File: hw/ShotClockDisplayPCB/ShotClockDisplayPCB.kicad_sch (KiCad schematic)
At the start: 0 parts

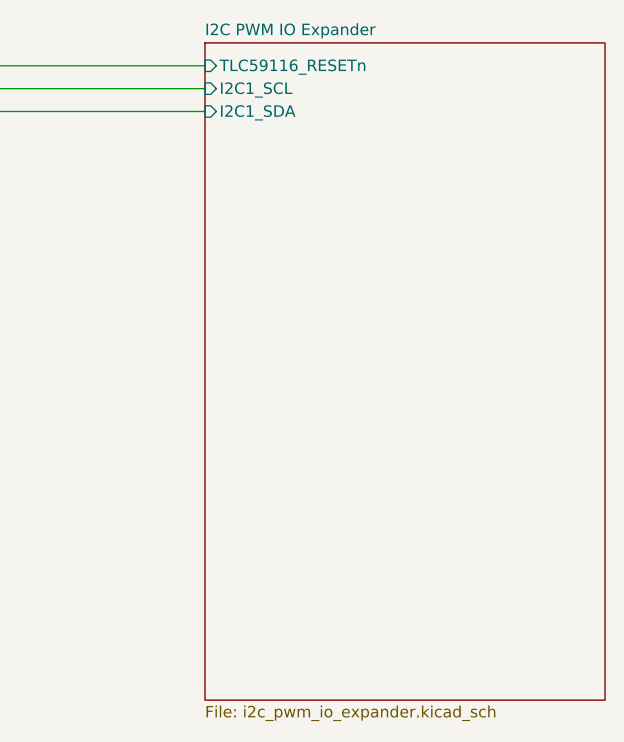
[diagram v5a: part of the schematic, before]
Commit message: Redid routing on disp PCB
Added TLC chip
Routed everything
Used way more filled areas
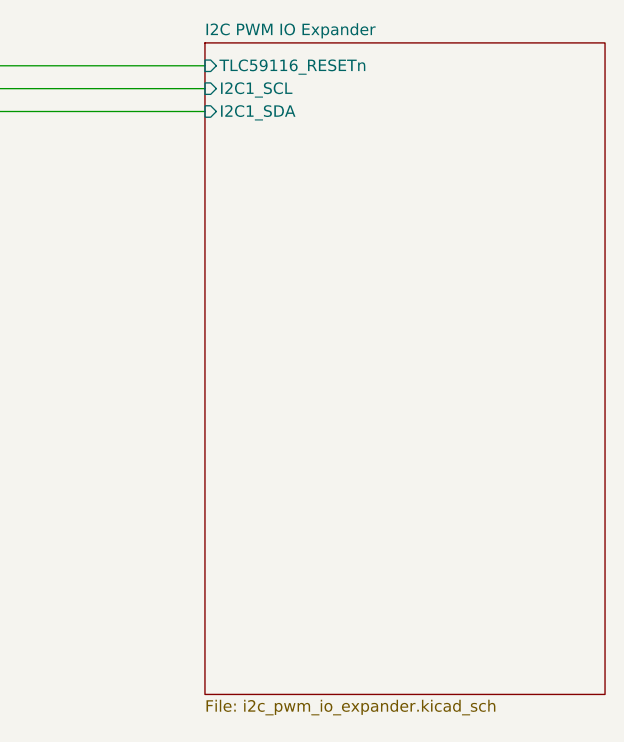
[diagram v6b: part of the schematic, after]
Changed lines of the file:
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@@
     )
   )
-  (sheet (at 140.335 54.61) (size 44.45 73.025) (fields_autoplaced)
+  (sheet (at 140.335 54.61) (size 44.45 72.39) (fields_autoplaced)
     (stroke (width 0.1524) (type solid))
     (fill (color 0 0 0 0.0000))
@@
       (effects (font (size 1.27 1.27)) (justify left bottom))
     )
-    (property "Sheetfile" "i2c_pwm_io_expander.kicad_sch" (at 140.335 128.2196 0)
+    (property "Sheetfile" "i2c_pwm_io_expander.kicad_sch" (at 140.335 127.5846 0)
       (effects (font (size 1.27 1.27)) (justify left top))
     )

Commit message: Fixed mainboard with feedback from Luc
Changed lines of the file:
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@@
     )
   )
-  (sheet (at 140.335 54.61) (size 44.45 72.39) (fields_autoplaced)
+  (sheet (at 140.335 54.61) (size 35.56 72.39) (fields_autoplaced)
     (stroke (width 0.1524) (type solid))
     (fill (color 0 0 0 0.0000))
@@
     )
   )
-  (sheet (at 77.47 54.61) (size 36.83 10.16) (fields_autoplaced)
+  (sheet (at 86.36 54.61) (size 27.94 10.16) (fields_autoplaced)
     (stroke (width 0.1524) (type solid))
     (fill (color 0 0 0 0.0000))
-    (property "Sheetname" "MainBoardConnectors" (at 77.47 53.8984 0)
+    (property "Sheetname" "MainBoardConnectors" (at 86.36 53.8984 0)
       (effects (font (size 1.27 1.27)) (justify left bottom))
     )
-    (property "Sheetfile" "mainboard_connectors.kicad_sch" (at 77.47 65.3546 0)
+    (property "Sheetfile" "mainboard_connectors.kicad_sch" (at 86.36 65.3546 0)
       (effects (font (size 1.27 1.27)) (justify left top))
     )
